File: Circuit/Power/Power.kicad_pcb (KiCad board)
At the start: 2 copper layers, 73.7 x 45.7 mm, 12 parts, among them J1 12V AC in, J2 To Flyback, J3 To Capacitors, J4 Signal, T1 Isolation, T2 Capacitor Charger, U1 S102S01

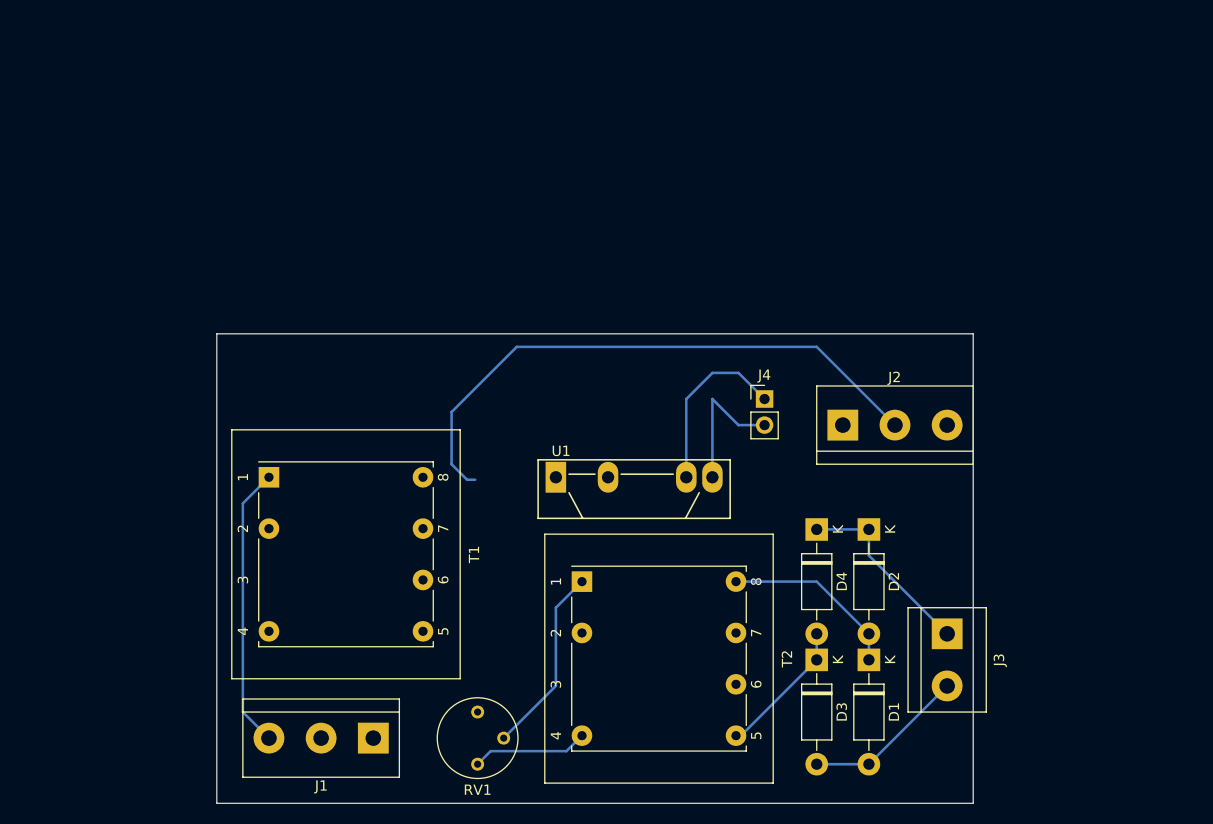
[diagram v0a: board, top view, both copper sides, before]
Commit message: [Circuit] Add customized footprint and symbol for transformers
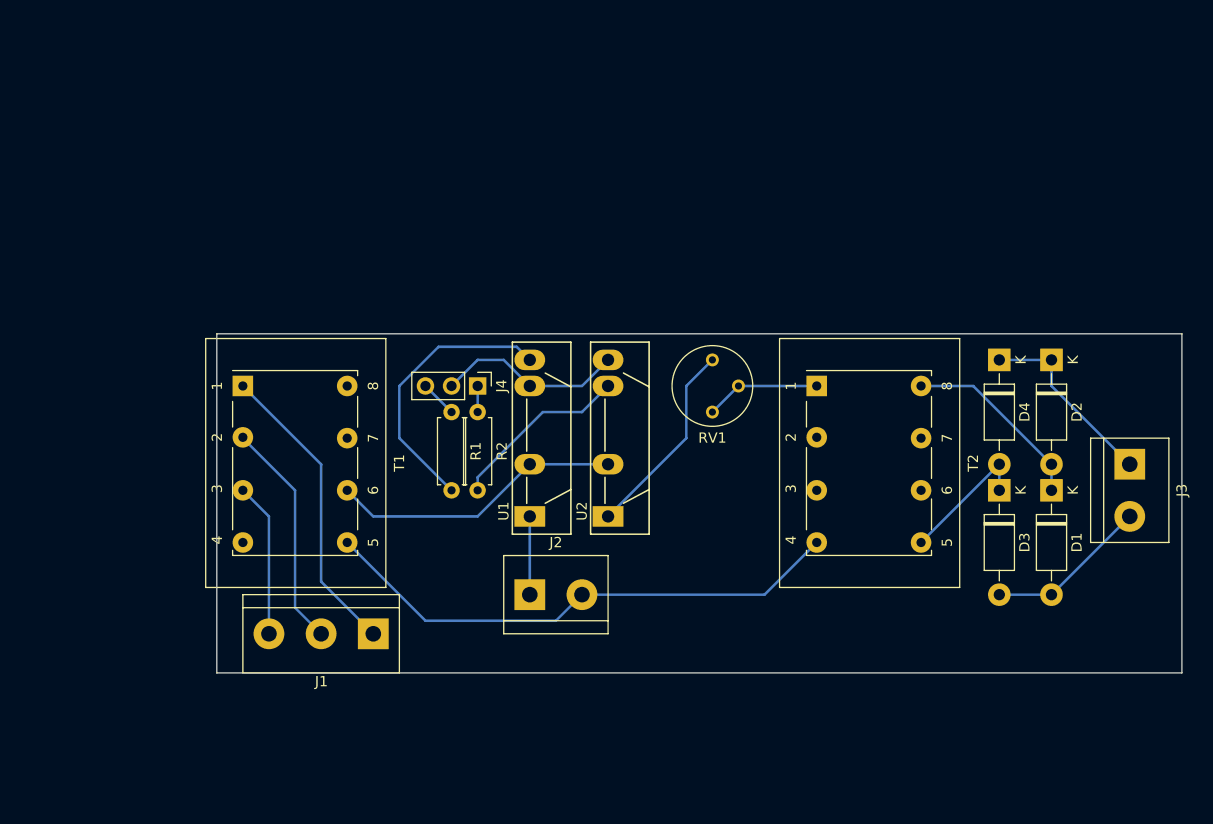
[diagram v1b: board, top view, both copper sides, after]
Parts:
- added R1: 1K, Resistor_THT:R_Axial_DIN0207_L6.3mm_D2.5mm_P7.62mm_Horizontal, F.Cu at (91.4, 58.4)
- added R2: 1K, Resistor_THT:R_Axial_DIN0207_L6.3mm_D2.5mm_P7.62mm_Horizontal, F.Cu at (94.0, 58.4)
- added U1: S102S01, Package_SIP:SIP4_Sharp-SSR_P7.62mm_Straight, F.Cu at (99.1, 68.6)
- J1: value 12V AC in -> +-12V Pulse in
- J2: value To Flyback -> To Starter; footprint TerminalBlock:TerminalBlock_bornier-3_P5.08mm -> TerminalBlock:TerminalBlock_bornier-2_P5.08mm
- J4: value Signal -> From Control; footprint Connector_PinHeader_2.54mm:PinHeader_1x02_P2.54mm_Vertical -> Connector_PinHeader_2.54mm:PinHeader_1x03_P2.54mm_Vertical
- RV1: value R_POT -> 50K
- T1: value Isolation -> 4+4:8; footprint Transformer_THT:Transformer_Breve_TEZ-22x24 -> Transformer_THT:Transformer_Generic_EE25_8Pin
- T2: value Capacitor Charger -> 6:200; footprint Transformer_THT:Transformer_Breve_TEZ-22x24 -> Transformer_THT:Transformer_Generic_EE25_8Pin
- moved RV1 41.2 mm to (116.8, 53.3)
- moved J2 34.7 mm to (99.1, 76.2)
- moved T2 29.8 mm to (127.0, 55.9)
- moved J4 28.0 mm to (94.0, 55.9), turned to 270 degrees
- moved J3 24.3 mm to (157.5, 63.5)
- moved D1 24.3 mm to (149.9, 66.0)
- moved D2 24.3 mm to (149.9, 53.3)
- moved D3 24.3 mm to (144.8, 66.0)
- moved D4 24.3 mm to (144.8, 53.3)
- moved J1 10.2 mm to (83.8, 80.0)
- moved T1 9.25 mm to (71.1, 55.9)
- moved U2 6.35 mm to (106.7, 68.6), turned to 90 degrees
- renumbered U1 to U2
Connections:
- net Net-(D1-Pad2) renamed /CapacitorPower-
- net Net-(D2-Pad1) renamed /CapacitorPower+
- net Net-(J1-Pad2) renamed /0Vin
- net Net-(J4-Pad2) renamed /ControlSignal
- J1 pad 1: Net-(J1-Pad1) -> /+12VPulseIn
- J1 pad 3: Net-(J1-Pad3) -> /-12VPulseIn
- J2 pad 1: Net-(J2-Pad1) -> /StarterPower+
- J2 pad 2: Net-(J2-Pad2) -> /StarterPower-
- J4 pad 1: Net-(J4-Pad1) -> /ControlPower
- RV1 pad 3: Net-(RV1-Pad3) -> Net-(RV1-Pad2)
- T1 pad 1: Net-(J1-Pad3) -> /+12VPulseIn
- T1 pad 4: Net-(T1-Pad4) -> (no net)
- T1 pad 5: Net-(J2-Pad2) -> /StarterPower-
- T1 pad 6: Net-(RV1-Pad1) -> Net-(T1-Pad6)
- T1 pad 7: Net-(RV1-Pad3) -> (no net)
- T2 pad 4: Net-(RV1-Pad3) -> /StarterPower-
- U2 pad 1: Net-(J2-Pad1) -> Net-(RV1-Pad1)
- U2 pad 2: Net-(T1-Pad4) -> Net-(T1-Pad6)
- U2 pad 3: Net-(J4-Pad1) -> Net-(R2-Pad2)
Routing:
- net Net-(J2-Pad2): track 57.0 -> 0.00 mm
- net /StarterPower-: track 0.00 -> 52.0 mm
- net /+12VPulseIn: track 0.00 -> 29.4 mm
- net Net-(T1-Pad6): track 0.00 -> 28.6 mm
- net Net-(J1-Pad3): track 27.5 -> 0.00 mm
- net Net-(R1-Pad2): track 0.00 -> 27.1 mm
- net /0Vin: track 0.00 -> 22.3 mm
- net Net-(RV1-Pad1): track 0.00 -> 19.4 mm
- net Net-(R2-Pad2): track 0.00 -> 17.7 mm
- net Net-(J4-Pad1): track 17.3 -> 0.00 mm
- net /-12VPulseIn: track 0.00 -> 15.0 mm
- net Net-(RV1-Pad3): track 11.3 -> 0.00 mm
- net /StarterPower+: track 0.00 -> 7.62 mm
- net Net-(RV1-Pad2): track 18.4 -> 11.2 mm
- net /ControlSignal: track 13.8 -> 18.4 mm
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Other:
- board size 73.7 x 45.7 mm -> 94 x 33 mm

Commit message: [Circuit] Use MOSFETs instead of TRIACs to control the powers
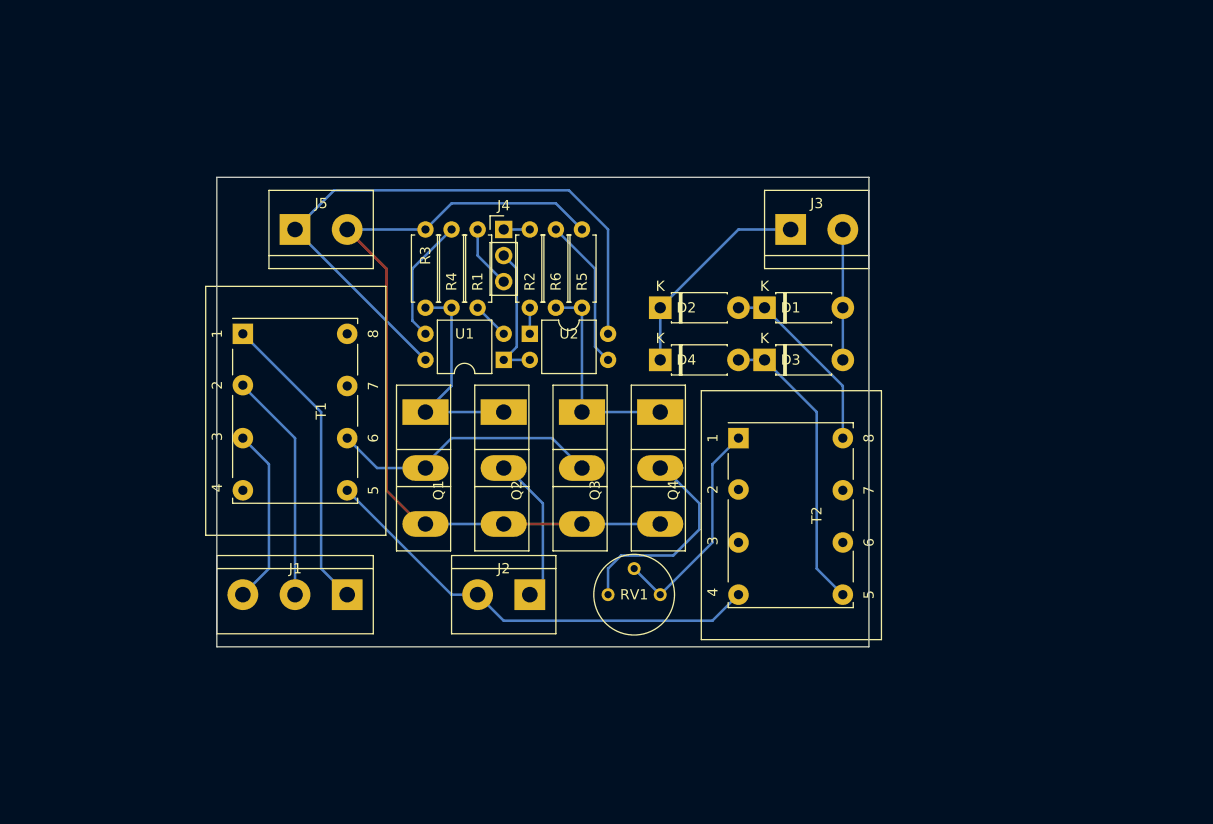
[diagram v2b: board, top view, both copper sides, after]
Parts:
- added J5: 12V DC in, TerminalBlock:TerminalBlock_bornier-2_P5.08mm, F.Cu at (76.2, 40.6)
- added Q1: IRFP250NPBF, Package_TO_SOT_THT:TO-247-3_Vertical, F.Cu at (88.9, 58.4)
- added Q2: IRFP250NPBF, Package_TO_SOT_THT:TO-247-3_Vertical, F.Cu at (96.5, 58.4)
- added Q3: IRFP250NPBF, Package_TO_SOT_THT:TO-247-3_Vertical, F.Cu at (104.1, 58.4)
- added Q4: IRFP250NPBF, Package_TO_SOT_THT:TO-247-3_Vertical, F.Cu at (111.8, 58.4)
- added R3: 10K, Resistor_THT:R_Axial_DIN0207_L6.3mm_D2.5mm_P7.62mm_Horizontal, F.Cu at (88.9, 40.6)
- added R4: 100, Resistor_THT:R_Axial_DIN0207_L6.3mm_D2.5mm_P7.62mm_Horizontal, F.Cu at (91.4, 40.6)
- added R5: 10K, Resistor_THT:R_Axial_DIN0207_L6.3mm_D2.5mm_P7.62mm_Horizontal, F.Cu at (104.1, 48.3)
- added R6: 100, Resistor_THT:R_Axial_DIN0207_L6.3mm_D2.5mm_P7.62mm_Horizontal, F.Cu at (101.6, 40.6)
- D1, D2, D3, D4: footprint Diode_THT:D_DO-41_SOD81_P10.16mm_Horizontal -> Diode_THT:D_DO-41_SOD81_P7.62mm_Horizontal
- U1, U2: value S102S01 -> PC817; footprint Package_SIP:SIP4_Sharp-SSR_P7.62mm_Straight -> Package_DIP:DIP-4_W7.62mm
- moved J3 40.2 mm to (124.5, 40.6), turned to 0 degrees
- moved D2 38.4 mm to (111.8, 48.3), turned to 0 degrees
- moved D1 33.1 mm to (121.9, 48.3), turned to 0 degrees
- moved D4 33.0 mm to (111.8, 53.3), turned to 0 degrees
- moved D3 26.2 mm to (121.9, 53.3), turned to 0 degrees
- moved RV1 25.0 mm to (106.7, 76.2), turned to 270 degrees
- moved U2 19.3 mm to (99.1, 50.8), turned to 0 degrees
- moved R2 18.5 mm to (99.1, 40.6)
- moved R1 18.0 mm to (94.0, 40.6)
- moved J4 15.5 mm to (96.5, 40.6), turned to 0 degrees
- moved U1 15.5 mm to (96.5, 53.3), turned to 180 degrees
- moved T2 9.16 mm to (119.4, 61.0)
- moved T1 5.08 mm to (71.1, 50.8)
- moved J1 4.58 mm to (81.3, 76.2)
- turned J2 to 180 degrees
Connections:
- RV1 pad 1: Net-(RV1-Pad1) -> Net-(Q4-Pad2)
- T1 pad 6: Net-(T1-Pad6) -> Net-(Q1-Pad2)
- U1 pad 1: /StarterPower+ -> /ControlSignal
- U1 pad 2: Net-(T1-Pad6) -> Net-(R1-Pad2)
- U1 pad 3: /ControlSignal -> Net-(R4-Pad1)
- U1 pad 4: Net-(R1-Pad2) -> +12V
- U2 pad 1: Net-(RV1-Pad1) -> Net-(R2-Pad2)
- U2 pad 2: Net-(T1-Pad6) -> /ControlSignal
- U2 pad 3: Net-(R2-Pad2) -> Net-(R6-Pad1)
- U2 pad 4: /ControlSignal -> +12V
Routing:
- net GND: track 0.00 -> 80.0 mm
- net +12V: track 0.00 -> 61.8 mm
- net Net-(T1-Pad6): track 28.6 -> 0.00 mm
- net Net-(Q1-Pad2): track 0.00 -> 26.7 mm
- net Net-(R1-Pad2): track 27.1 -> 3.59 mm
- net Net-(Q4-Pad2): track 0.00 -> 23.0 mm
- net Net-(Q1-Pad1): track 0.00 -> 21.4 mm
- net Net-(Q3-Pad1): track 0.00 -> 20.3 mm
- net Net-(RV1-Pad1): track 19.4 -> 0.00 mm
- net Net-(D3-Pad1): track 13.3 -> 28.6 mm
- net Net-(R2-Pad2): track 17.7 -> 2.54 mm
- net Net-(R6-Pad1): track 0.00 -> 14.8 mm
- net Net-(R4-Pad1): track 0.00 -> 12.3 mm
- net Net-(RV1-Pad2): track 11.2 -> 22.0 mm
- net /StarterPower-: track 52.0 -> 44.4 mm
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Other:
- board size 94 x 33 mm -> 63.5 x 45.7 mm

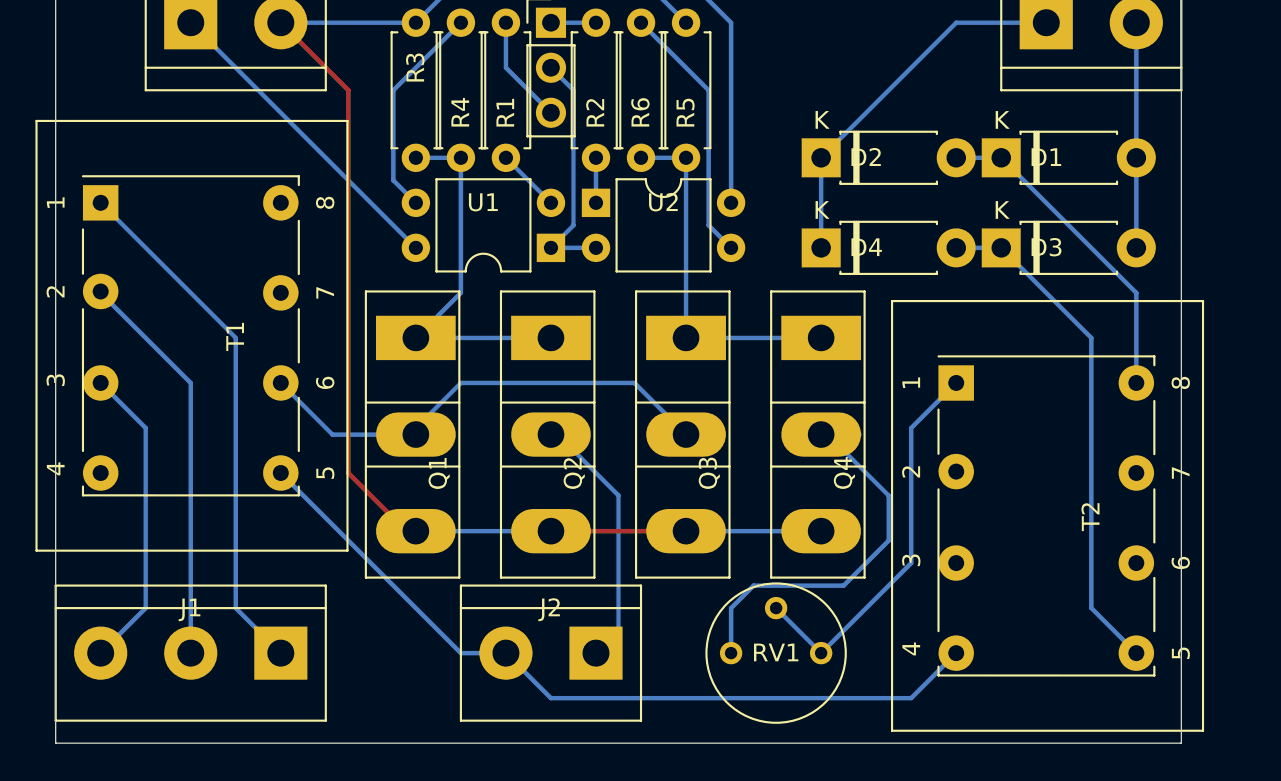
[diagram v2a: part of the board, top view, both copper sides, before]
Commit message: [Circuit] More accurate on the dimension of transformers
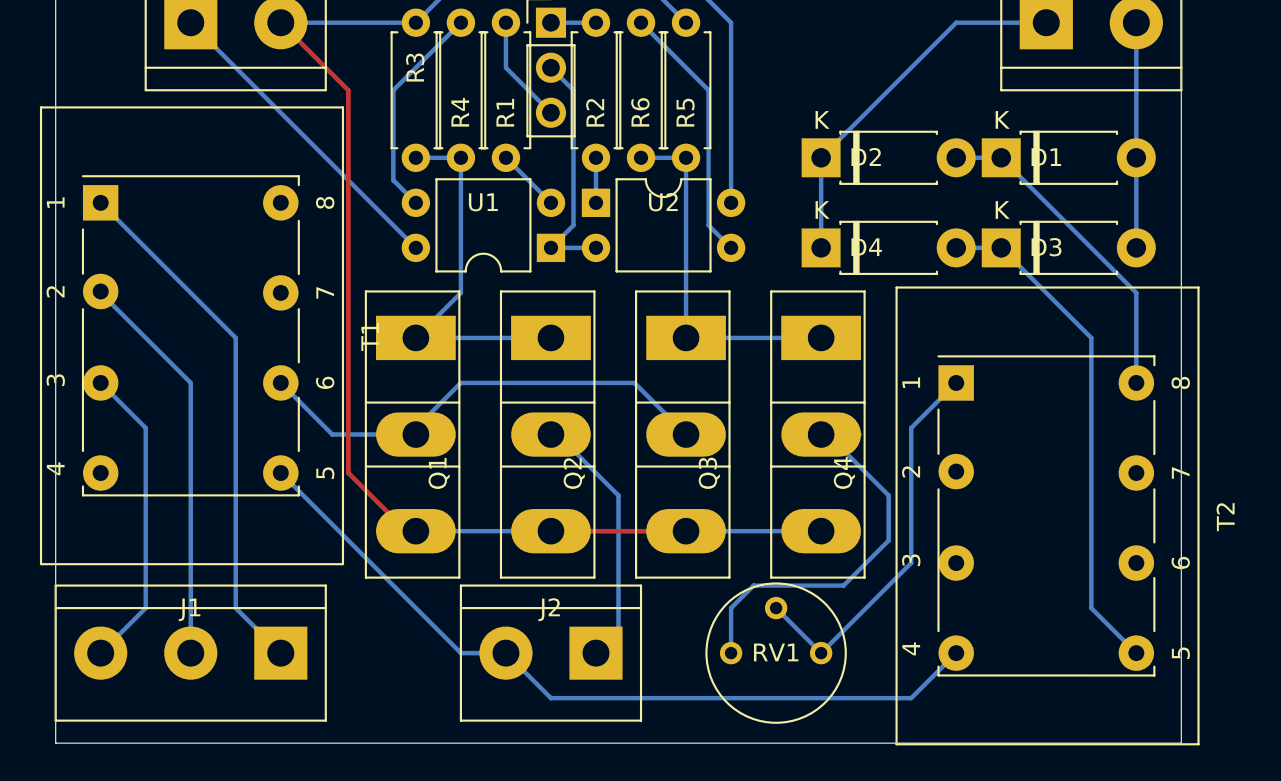
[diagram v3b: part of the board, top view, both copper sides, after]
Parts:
- T1, T2: footprint Transformer_THT:Transformer_Generic_EE25_8Pin -> Power:Transformer_Generic_EE25_8Pin

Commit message: [Circuit] Move the Nozzle's MOSFET to power module
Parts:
- added Q5: IRFP250NPBF, Package_TO_SOT_THT:TO-247-3_Vertical, F.Cu at (88.9, 58.4)
- J2: value To Starter -> To Starter & Coil; footprint TerminalBlock:TerminalBlock_bornier-2_P5.08mm -> TerminalBlock:TerminalBlock_bornier-3_P5.08mm
- moved T2 15.2 mm to (134.6, 61.0)
- moved D1 15.2 mm to (137.2, 48.3)
- moved D2 15.2 mm to (127.0, 48.3)
- moved D3 15.2 mm to (137.2, 53.3)
- moved D4 15.2 mm to (127.0, 53.3)
- moved J3 15.2 mm to (139.7, 40.6)
- moved Q2 7.62 mm to (104.1, 58.4)
- moved Q3 7.62 mm to (111.8, 58.4)
- moved Q1 7.62 mm to (96.5, 58.4)
- moved Q4 7.62 mm to (119.4, 58.4)
- moved RV1 5.08 mm to (101.6, 76.2)
- moved J2 2.54 mm to (96.5, 76.2)
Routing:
- net /StarterPower-: track 44.4 -> 67.0 mm
- net Net-(RV1-Pad2): track 22.0 -> 37.8 mm
- net /CoilControl: track 0.00 -> 15.0 mm
- net Net-(Q1-Pad1): track 21.4 -> 29.0 mm
- net Net-(Q1-Pad2): track 26.7 -> 34.3 mm
- net GND: track 80.0 -> 87.6 mm
- net Net-(Q3-Pad1): track 20.3 -> 25.0 mm
- net Net-(Q4-Pad2): track 23.0 -> 26.4 mm
- net +12V: track 61.8 -> 63.2 mm
- net /StarterPower+: track 14.7 -> 16.1 mm
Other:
- board size 63.5 x 45.7 mm -> 78.7 x 45.7 mm
